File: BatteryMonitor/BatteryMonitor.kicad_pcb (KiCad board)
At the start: 4 copper layers, 40 x 40 mm, 61 parts, among them J1 SWD, J2 BAT+, J3 BAL_THERM, J4 I2C, J5 BAT-, J6 PACK_OUT, Q1 NTMFS0D6N04XM, Q2 NTMFS0D6N04XM, SW1 WAKE, U1 BQ76905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

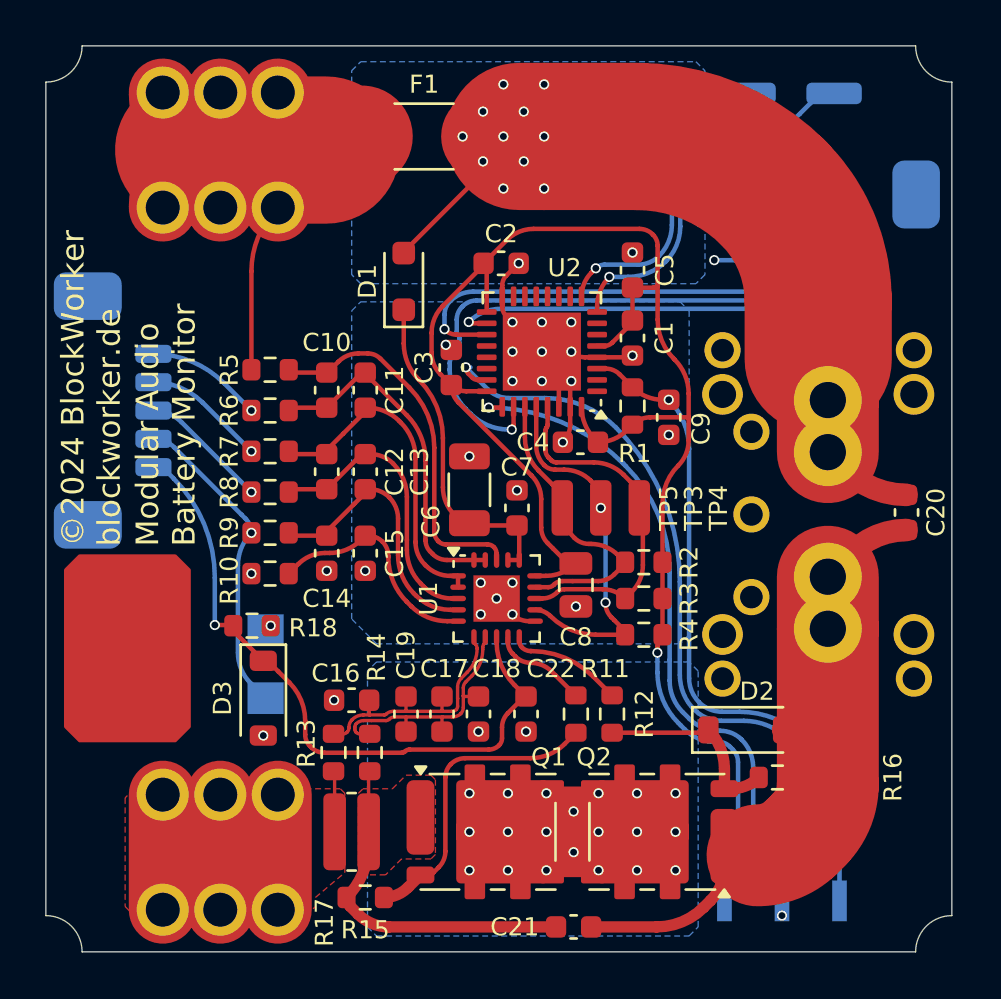
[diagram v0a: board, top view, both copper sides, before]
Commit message: BatteryMonitor added power switch connector
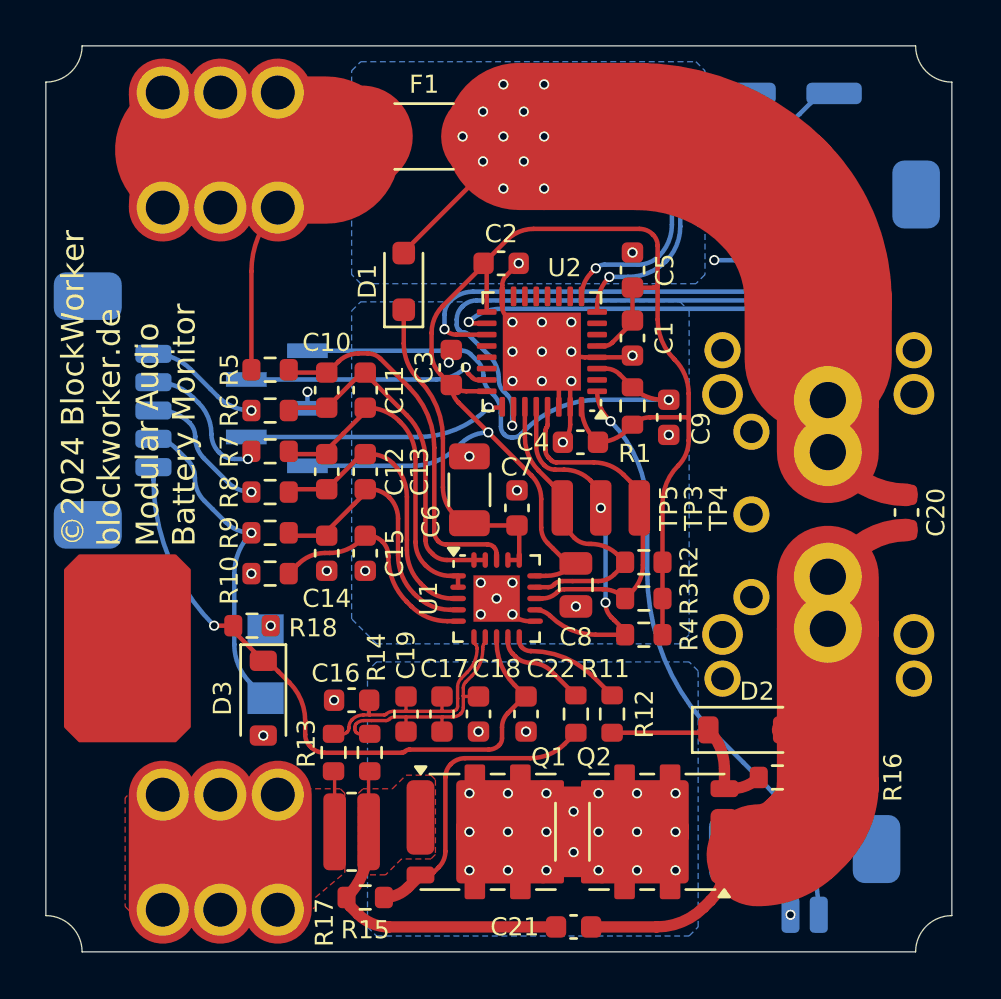
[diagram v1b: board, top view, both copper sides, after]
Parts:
- added J7: PWR_SWITCH, BW_Connectors:Amphenol_MINITEK_WTB_1.25_2P, B.Cu at (163.5, 115.9)
- moved J1 30.2 mm to (140.2, 96.0), turned to 0 degrees
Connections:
- U2 pad 1: unconnected-(U2-PC14-Pad1) -> /PWR_SWITCH
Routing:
- net /PWR_SWITCH: track 0.00 -> 25.9 mm, vias 0 -> 1
- net /SWDIO: track 31.4 -> 11.0 mm
- net /SWCLK: track 26.3 -> 11.6 mm
- net Net-(J1-Pin_5): track 29.9 -> 22.6 mm
- net +3.3V: track 73.4 -> 68.0 mm
- net GND: track 32.9 -> 34.2 mm, vias 32 -> 33
- net /SDA_EXT: track 25.5 -> 24.4 mm
- net Net-(J3-Pin_2): track 5.44 -> 6.40 mm
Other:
- board text added: "PWR"
